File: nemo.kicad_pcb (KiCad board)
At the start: 2 copper layers, 69.7 x 24.5 mm, 20 parts, among them J1 Conn_01x02_Male, J2 Conn_01x06_Male, J3 Conn_01x02_Male, J4 Conn_01x06_Male, J5 Conn_02x03_Odd_Even, J6 Conn_01x12_Male, SW1 SW_Push, U1 ATmega328P-AU, U2 L7805, Y1 16MHz

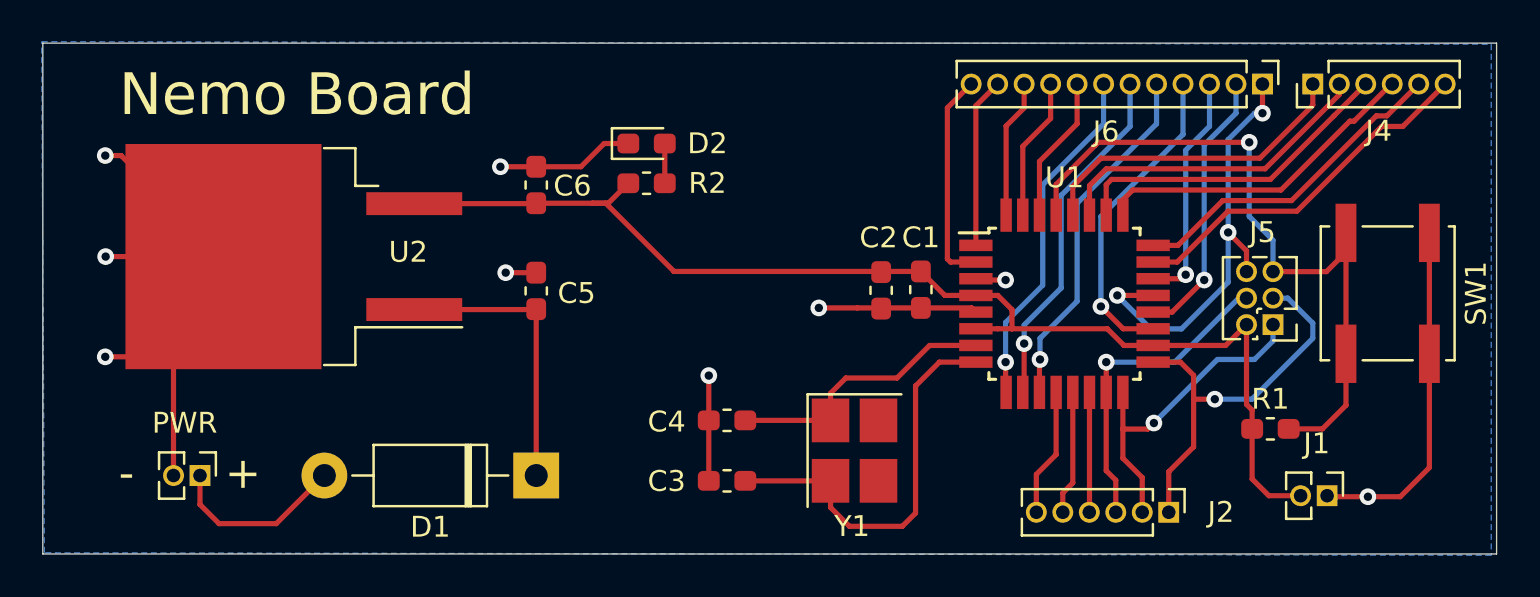
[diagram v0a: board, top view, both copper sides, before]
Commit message: * Added README.md * Added BOM - bom.csv * Exportet schematic to pdf - schematic.pdf
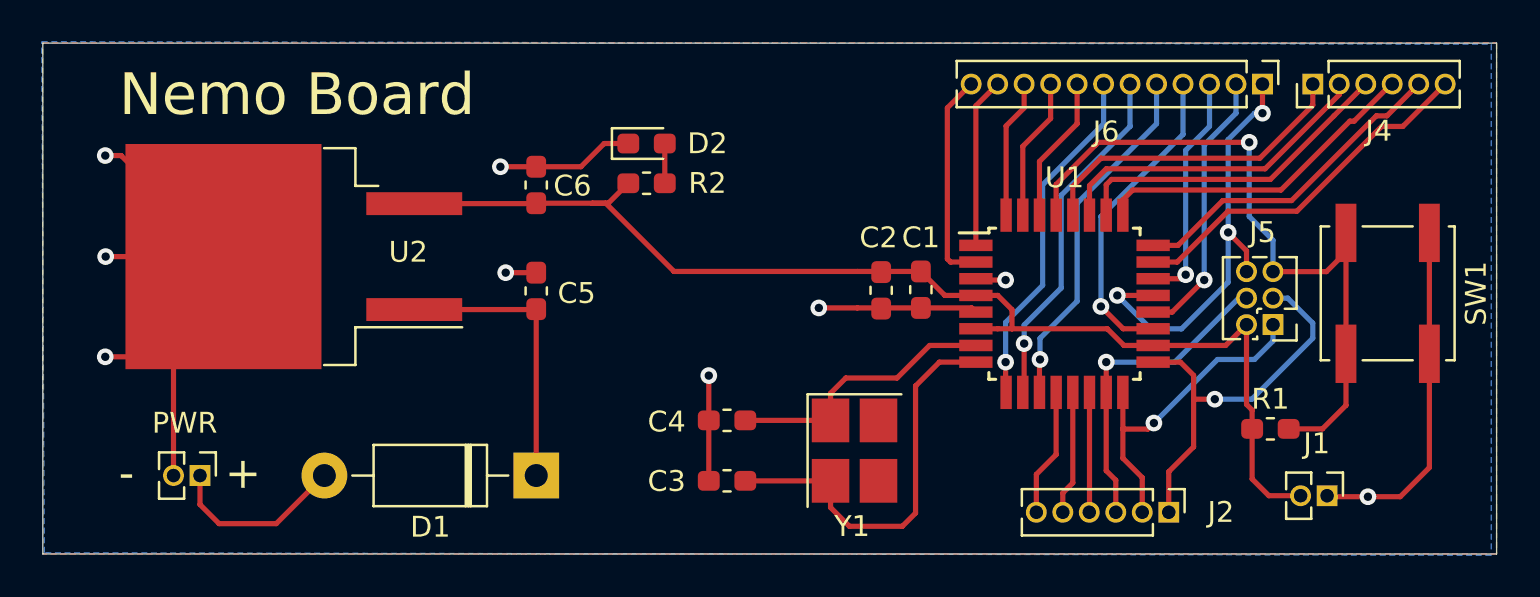
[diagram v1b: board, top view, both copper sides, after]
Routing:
- added copper zone on F.Cu, net GND
